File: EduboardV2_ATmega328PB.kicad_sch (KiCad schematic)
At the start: 9 parts, among them J1 EduboardV2 PCIE UP Board Conn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, SW1 K2-1102SP-C4SC-04, U2 ATMEGA328PB-AUR

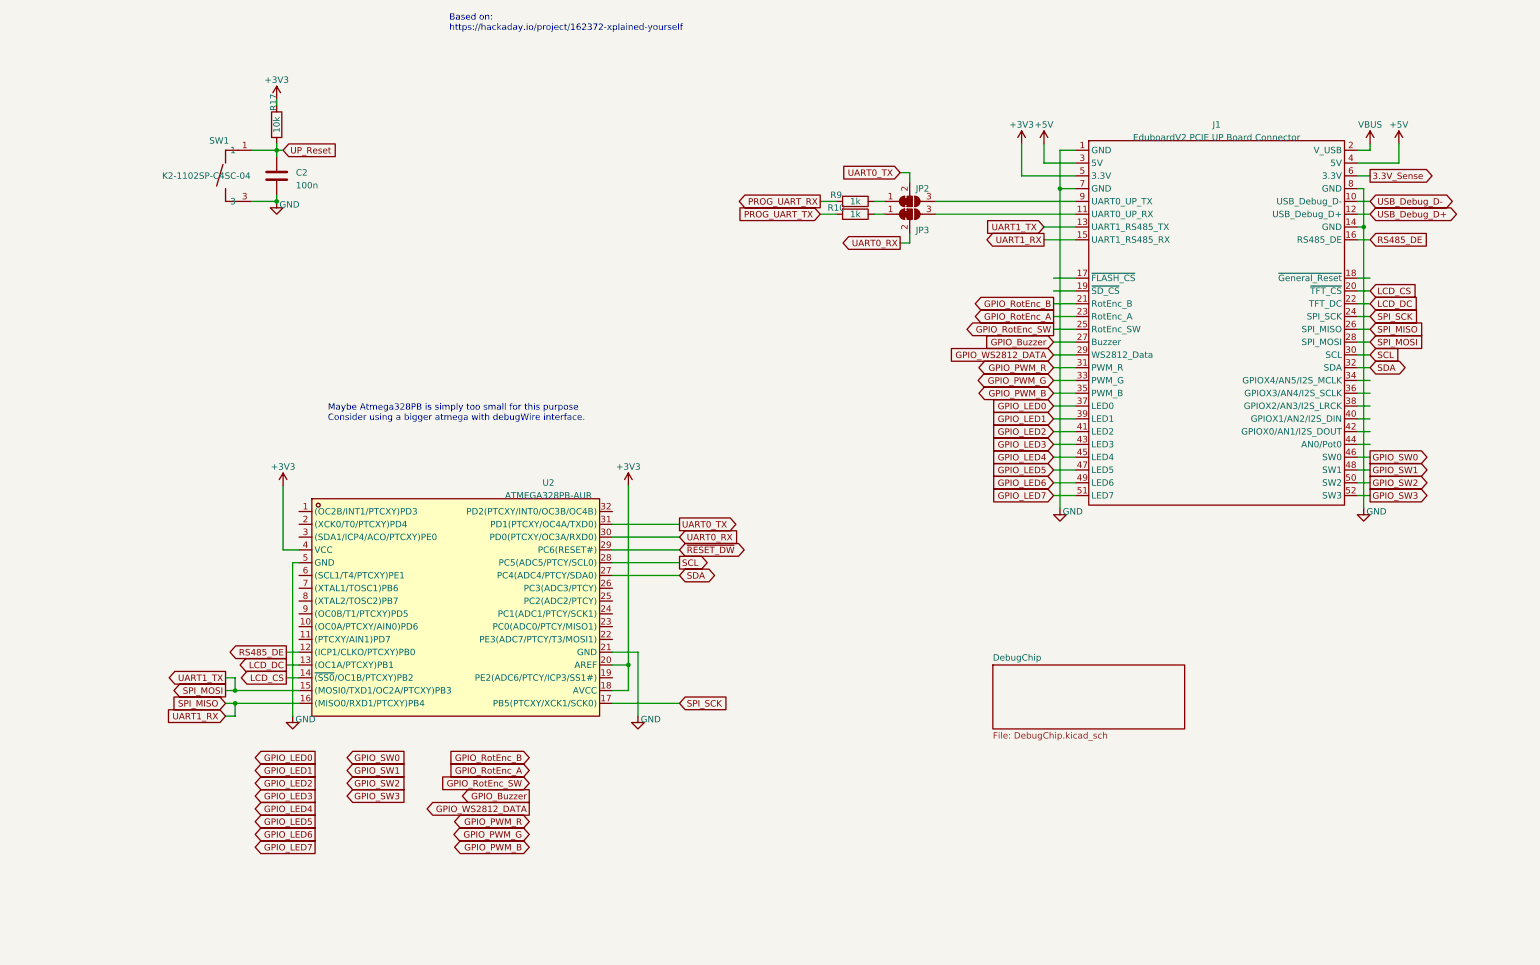
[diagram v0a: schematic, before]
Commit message: start distribute pins to signals.
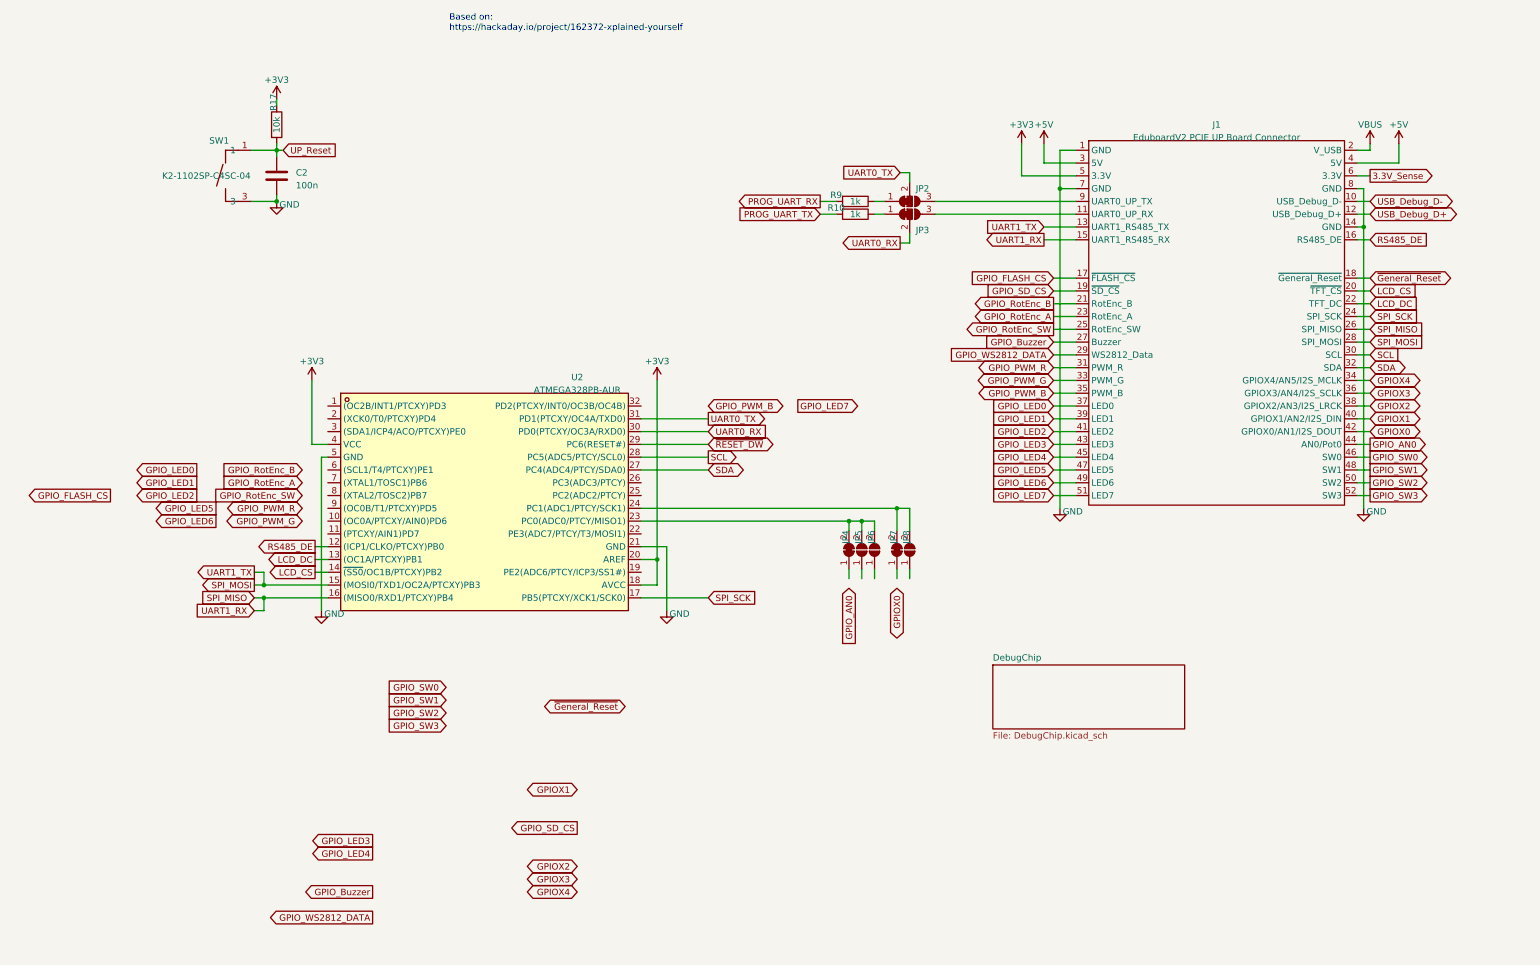
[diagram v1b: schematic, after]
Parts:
- added JP4, JP7: SolderJumper_2_Bridged, symbol Jumper:SolderJumper_2_Bridged
- added JP5, JP6, JP8: SolderJumper_2_Open, symbol Jumper:SolderJumper_2_Open
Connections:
- net GPIO_FLASH_CS: now reaches J1.17 (~{FLASH_CS})
- net ~{General_Reset}: now reaches J1.18 (~{General_Reset})
- net GPIO_SD_CS: now reaches J1.19 (~{SD_CS})
- net GPIOX4: now reaches J1.34 (GPIOX4/AN5/I2S_MCLK)
- net GPIOX3: now reaches J1.36 (GPIOX3/AN4/I2S_SCLK)
- net GPIOX2: now reaches J1.38 (GPIOX2/AN3/I2S_LRCK)
- net GPIOX1: now reaches J1.40 (GPIOX1/AN2/I2S_DIN)
- net GPIOX0: now reaches J1.42 (GPIOX0/AN1/I2S_DOUT)
- net GPIO_AN0: now reaches J1.44 (AN0/Pot0)
- net at U2.23 (PC0(ADC0/PTCY/MISO1)): now also JP4.2 (B), JP5.2 (B), JP6.2 (B)
- net at U2.24 (PC1(ADC1/PTCY/SCK1)): now also JP7.2 (B), JP8.2 (B)
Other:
- note removed: "Maybe Atmega328PB is simply too small for this purpose Consider using a bigger atmega with debugWire interface."
- moved on the sheet: U2

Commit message: schematic done. layout done aswell. Have to check everything trice
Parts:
- removed C2: 100n, Capacitor_SMD:C_0603_1608Metric, symbol Device:C
- removed JP4, JP7: SolderJumper_2_Bridged, symbol Jumper:SolderJumper_2_Bridged
- removed JP5, JP6, JP8: SolderJumper_2_Open, symbol Jumper:SolderJumper_2_Open
- added C1 (x3): 100n, Capacitor_SMD:C_0402_1005Metric, symbol Device:C
- added JP16, JP17, JP18, JP19, JP20, JP21, JP22, JP30, JP34, JP5, JP6, JP7: SolderJumper_3_Bridged12, EduboardV2_kicadlib:SolderJumper_Small-3_bridged12, symbol EduboardV2_kicadlib:SolderJumper_Small_3_Bridged12
- added JP23, JP4: SolderJumper_3_Bridged12, EduboardV2_kicadlib:SolderJumper_Small-4_bridged14, symbol EduboardV2_kicadlib:SolderJumper_Small_4_Bridged14
- JP2, JP3: footprint (none) -> EduboardV2_kicadlib:SolderJumper_Small-3_bridged12
- R10, R17, R9: footprint Resistor_SMD:R_0603_1608Metric -> Resistor_SMD:R_0402_1005Metric
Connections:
- net UP_Reset is gone; now on net ~{RESET_DW}: R17.2, SW1.1, SW1.2
- net +3V3: now also C1.1, C1.1, C1.1
- net GND: now also C1.2, C1.2, C1.2
- net GPIOX0: now also JP4.2 (A)
- net GPIOX1: now also JP5.3 (B)
- net GPIOX2: now also JP6.3 (B)
- net GPIOX3: now also JP23.3 (B)
- net GPIOX4: now also JP16.3 (B)
- net GPIO_AN0: now also JP23.1 (A)
- net GPIO_Buzzer: now also JP20.1 (A)
- net GPIO_FLASH_CS: now also JP4.3 (B)
- net GPIO_LED0: now also U2.1 ((OC2B/INT1/PTCXY)PD3)
- net GPIO_LED1: now also U2.2 ((XCK0/T0/PTCXY)PD4)
- net GPIO_LED2: now also U2.3 ((SDA1/ICP4/ACO/PTCXY)PE0)
- net GPIO_LED3: now also JP21.1 (A)
- net GPIO_LED4: now also JP17.1 (A)
- net GPIO_LED5: now also JP19.1 (A)
- net GPIO_LED6: now also JP18.1 (A)
- net GPIO_LED7: now also JP7.1 (A)
- net GPIO_PWM_B: now also JP7.3 (B)
- net GPIO_PWM_G: now also JP18.3 (B)
- net GPIO_PWM_R: now also JP19.3 (B)
- net GPIO_RotEnc_A: now also JP17.3 (B)
- net GPIO_RotEnc_B: now also JP21.3 (B)
- net GPIO_RotEnc_SW: now also JP20.3 (B)
- net GPIO_SD_CS: now also JP23.2 (A)
- net GPIO_SW0: now also U2.19 (PE2(ADC6/PTCY/ICP3/SS1#))
- net GPIO_SW1: now also U2.22 (PE3(ADC7/PTCY/T3/MOSI1))
- net GPIO_SW2: now also JP5.1 (A)
- net GPIO_SW3: now also JP6.1 (A)
- net GPIO_WS2812_DATA: now also U2.11 ((PTCXY/AIN1)PD7)
- net LCD_DC: now also JP16.1 (A); no longer U2.13 ((OC1A/PTCXY)PB1)
- net RS485_DE: now also JP22.3 (B); no longer U2.12 ((ICP1/CLKO/PTCXY)PB0)
- net SPI_MISO: now also JP34.3 (B); no longer J1.15 (UART1_RS485_RX), U2.16 ((MISO0/RXD1/PTCXY)PB4)
- net SPI_MOSI: now also JP30.1 (A); no longer J1.13 (UART1_RS485_TX), U2.15 ((MOSI0/TXD1/OC2A/PTCXY)PB3)
- net ~{General_Reset}: now also JP4.1 (A)
- net at U2.24 (PC1(ADC1/PTCY/SCK1)): now also JP4.4 (C)
- net at U2.23 (PC0(ADC0/PTCY/MISO1)): now also JP23.4 (C)
- net at U2.10 ((OC0A/PTCXY/AIN0)PD6): now also JP18.2 (C)
- net at U2.25 (PC2(ADC2/PTCY)): now also JP5.2 (C)
- net at U2.26 (PC3(ADC3/PTCY)): now also JP6.2 (C)
- net at U2.32 (PD2(PTCXY/INT0/OC3B/OC4B)): now also JP7.2 (C)
- net at U2.6 ((SCL1/T4/PTCXY)PE1): now also JP21.2 (C)
- net at U2.7 ((XTAL1/TOSC1)PB6): now also JP22.2 (C)
- net at U2.8 ((XTAL2/TOSC2)PB7): now also JP20.2 (C)
- net at U2.9 ((OC0B/T1/PTCXY)PD5): now also JP19.2 (C)
- new net: JP30.2 (C), U2.15 ((MOSI0/TXD1/OC2A/PTCXY)PB3)
- new net: JP17.2 (C), U2.12 ((ICP1/CLKO/PTCXY)PB0)
- new net: JP16.2 (C), U2.13 ((OC1A/PTCXY)PB1)
- new net: JP34.2 (C), U2.16 ((MISO0/RXD1/PTCXY)PB4)
- new net EXT_CLK: JP22.1 (A)
- new net UART1_RX: J1.15 (UART1_RS485_RX), JP34.1 (A)
- new net UART1_TX: J1.13 (UART1_RS485_TX), JP30.3 (B)
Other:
- moved on the sheet: J1, JP2, JP3, R10, R17, R9, SW1, U2

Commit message: got first prototypes. Found some errors. not yet corrected, but marked.
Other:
- note added: "Fehler MISO/UART default falsch"
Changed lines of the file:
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@@
     (effects (font (size 1.27 1.27)) (justify left bottom))
+  )
+  (text "Fehler\nMISO/UART default falsch\n" (at 67.31 168.91 90)
+    (effects (font (size 1.27 1.27) (color 255 0 0 1)) (justify right bottom))
   )
   (global_label "USB_Debug_D+" (shape bidirectional) (at 264.16 33.02 0) (fields_autoplaced)

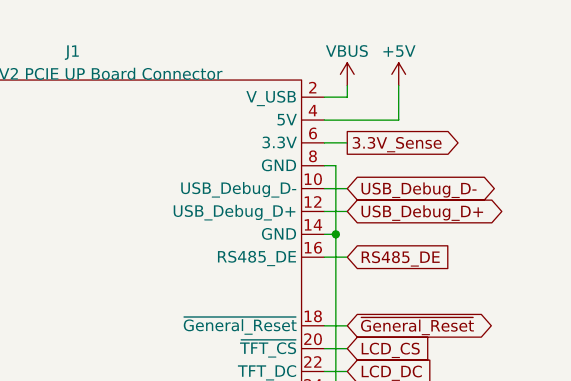
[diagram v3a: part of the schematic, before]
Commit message: remove voltage regulator and change sense input to 3.3V
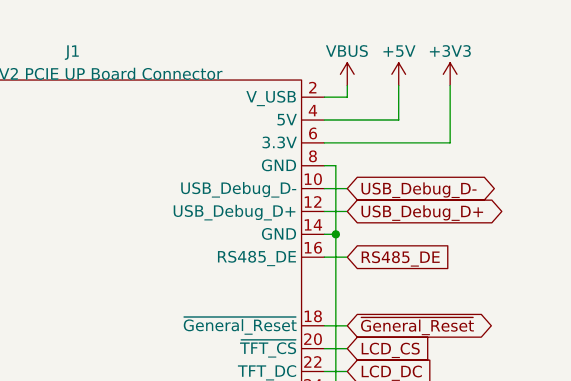
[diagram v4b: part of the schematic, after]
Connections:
- net 3.3V_Sense is gone; now on net +3V3: J1.6 (3.3V)
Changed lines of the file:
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@@
+    (stroke (width 0) (type default))
+  )
+  (wire (pts (xy 275.59 19.05) (xy 275.59 25.4))
     (stroke (width 0) (type default))
   )
@@
     (stroke (width 0) (type default))
   )
-  (wire (pts (xy 261.62 25.4) (xy 264.16 25.4))
+  (wire (pts (xy 261.62 25.4) (xy 275.59 25.4))
     (stroke (width 0) (type default))
   )
@@
     (property "Intersheetrefs" "${INTERSHEET_REFS}" (at 185.4246 68.58 0)
       (effects (font (size 1.27 1.27)) (justify right) hide)
-    )
-  )
-  (global_label "3.3V_Sense" (shape output) (at 264.16 25.4 0) (fields_autoplaced)
-    (effects (font (size 1.27 1.27)) (justify left))
-    (property "Intersheetrefs" "${INTERSHEET_REFS}" (at 277.7096 25.4 0)
-      (effects (font (size 1.27 1.27)) (justify left) hide)
     )
   )
@@
         )
       )
+    )
+  )
+  (symbol (lib_id "power:+3V3") (at 275.59 19.05 0) (unit 1)
+    (in_bom yes) (on_board yes) (dnp no) (fields_autoplaced)
+    (property "Reference" "#PWR04" (at 275.59 22.86 0)
+      (effects (font (size 1.27 1.27)) hide)
+    )
+    (property "Value" "+3V3" (at 275.59 15.24 0)
+      (effects (font (size 1.27 1.27)))
+    )
+    (property "Footprint" "" (at 275.59 19.05 0)
+      (effects (font (size 1.27 1.27)) hide)
+    )
+    (property "Datasheet" "" (at 275.59 19.05 0)
+      (effects (font (size 1.27 1.27)) hide)
+    )
+    (pin "1")
+    (instances
+      (project "EduboardV2_ATmega328PB"
+        (path "/0ef5f433-62f3-413e-ac2a-aa07749066ac/83d3690c-6ff2-4209-82b8-d055572b14ab"
+          (reference "#PWR04") (unit 1)
+        )
+        (path "/0ef5f433-62f3-413e-ac2a-aa07749066ac"
+          (reference "#PWR041") (unit 1)
+        )
+      )

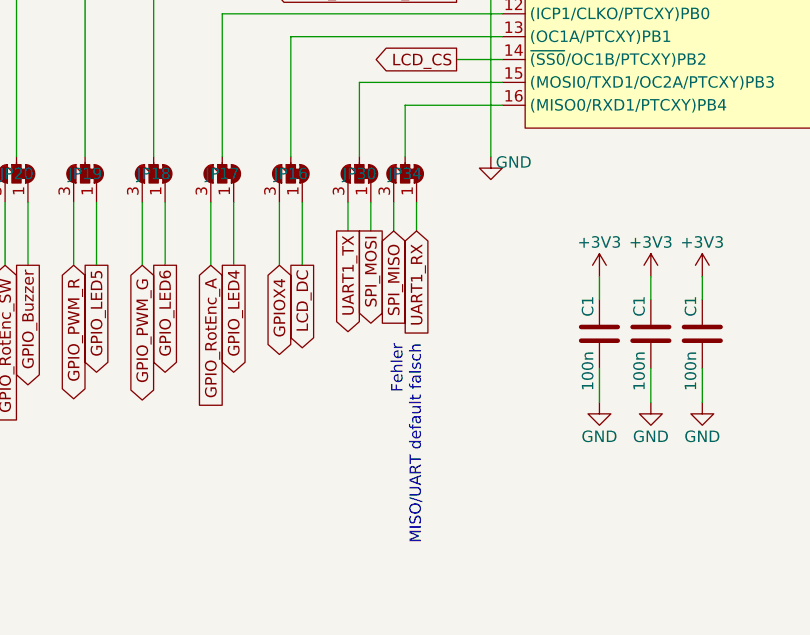
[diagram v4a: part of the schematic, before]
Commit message: switch default routing of j34 miso/uart_rx
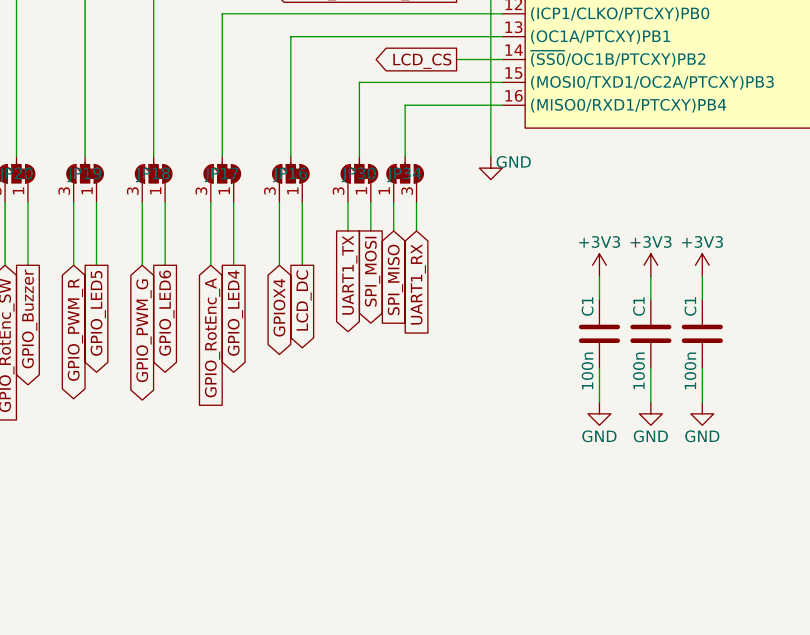
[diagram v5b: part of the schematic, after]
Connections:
- net SPI_MISO: now also JP34.1 (A); no longer JP34.3 (B)
- net UART1_RX: now also JP34.3 (B); no longer JP34.1 (A)
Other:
- note removed: "Fehler MISO/UART default falsch"
- moved on the sheet: JP34
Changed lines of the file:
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@@
     (effects (font (size 1.27 1.27)) (justify left bottom))
-  )
-  (text "Fehler\nMISO/UART default falsch\n" (at 67.31 168.91 90)
-    (effects (font (size 1.27 1.27) (color 255 0 0 1)) (justify right bottom))
   )
   (global_label "USB_Debug_D+" (shape bidirectional) (at 264.16 33.02 0) (fields_autoplaced)
@@
     )
   )
-  (symbol (lib_id "EduboardV2_kicadlib:SolderJumper_Small_3_Bridged12") (at 65.405 149.86 270) (mirror x) (unit 1)
-    (in_bom yes) (on_board yes) (dnp no)
-    (property "Reference" "JP34" (at 67.31 149.86 90)
+  (symbol (lib_id "EduboardV2_kicadlib:SolderJumper_Small_3_Bridged12") (at 65.405 149.86 90) (unit 1)
+    (in_bom yes) (on_board yes) (dnp no)
+    (property "Reference" "JP34" (at 63.5 149.86 90)
       (effects (font (size 1.27 1.27)) (justify right))
     )
-    (property "Value" "SolderJumper_3_Bridged12" (at 72.39 149.86 0)
-      (effects (font (size 1.27 1.27)) hide)
-    )
-    (property "Footprint" "EduboardV2_kicadlib:SolderJumper_Small-3_bridged12" (at 58.42 150.495 0)
-      (effects (font (size 1.27 1.27)) hide)
-    )
+    (property "Value" "SolderJumper_3_Bridged12" (at 58.42 149.86 0)
+      (effects (font (size 1.27 1.27)) hide)
+    )
+    (property "Footprint" "EduboardV2_kicadlib:SolderJumper_Small-3_bridged12" (at 72.39 150.495 0)
+      (effects (font (size 1.27 1.27)) hide)
+    )

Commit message: arrange parts and layout v1.1.
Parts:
- removed JP16, JP17, JP18, JP19, JP20, JP21, JP22, JP30, JP34, JP5, JP6, JP7: SolderJumper_3_Bridged12, EduboardV2_kicadlib:SolderJumper_Small-3_bridged12, symbol EduboardV2_kicadlib:SolderJumper_Small_3_Bridged12
- removed JP2, JP3: SolderJumper_3_Bridged12, EduboardV2_kicadlib:SolderJumper_Small-3_bridged12, symbol Jumper:SolderJumper_3_Bridged12
- removed JP23, JP4: SolderJumper_3_Bridged12, EduboardV2_kicadlib:SolderJumper_Small-4_bridged14, symbol EduboardV2_kicadlib:SolderJumper_Small_4_Bridged14
- added R3 (x32): 0R, Resistor_SMD:R_0603_1608Metric, symbol Device:R
- renumbered U2 to U1
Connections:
- net EXT_CLK: now also R3.1
- net GPIOX0: now also R3.2
- net GPIOX1: now also R3.2
- net GPIOX2: now also R3.2
- net GPIOX3: now also R3.2
- net GPIOX4: now also R3.2
- net GPIO_AN0: now also R3.2
- net GPIO_Buzzer: now also R3.2
- net GPIO_FLASH_CS: now also R3.2
- net GPIO_LED3: now also R3.1
- net GPIO_LED4: now also R3.2
- net GPIO_LED5: now also R3.2
- net GPIO_LED6: now also R3.2
- net GPIO_LED7: now also R3.1
- net GPIO_PWM_B: now also R3.1
- net GPIO_PWM_G: now also R3.2
- net GPIO_PWM_R: now also R3.2
- net GPIO_RotEnc_A: now also R3.2
- net GPIO_RotEnc_B: now also R3.1
- net GPIO_RotEnc_SW: now also R3.2
- net GPIO_SD_CS: now also R3.2
- net GPIO_SW2: now also R3.2
- net GPIO_SW3: now also R3.2
- net LCD_DC: now also R3.2
- net RS485_DE: now also R3.1
- net SPI_MISO: now also R3.2
- net SPI_MOSI: now also R3.2
- net UART0_RX: now also R10.1, R3.1
- net UART0_TX: now also R9.1, R3.1
- net UART1_RX: now also R3.2
- net UART1_TX: now also R3.2
- net ~{General_Reset}: now also R3.2
- net UP_SPI_MOSI: now reaches U1.15 ((MOSI0/TXD1/OC2A/PTCXY)PB3)
- net UP_SPI_MOSI: now also R3.1, R3.1
- net at U1.24 (PC1(ADC1/PTCY/SCK1)): now also R3.1, R3.1, R3.1
- net at U1.12 ((ICP1/CLKO/PTCXY)PB0): now also R3.1, R3.1
- net at J1.9 (UART0_UP_TX): now also R3.2
- net at J1.11 (UART0_UP_RX): now also R3.2
- net at U1.26 (PC3(ADC3/PTCY)): now also R3.1, R3.1
- net at U1.32 (PD2(PTCXY/INT0/OC3B/OC4B)): now also R3.2, R3.2
- net at U1.10 ((OC0A/PTCXY/AIN0)PD6): now also R3.1, R3.1
- net at U1.13 ((OC1A/PTCXY)PB1): now also R3.1, R3.1
- net UP_SPI_MISO: now reaches U1.16 ((MISO0/RXD1/PTCXY)PB4)
- net UP_SPI_MISO: now also R3.1, R3.1
- net at U1.23 (PC0(ADC0/PTCY/MISO1)): now also R3.1, R3.1, R3.1
- net at U1.25 (PC2(ADC2/PTCY)): now also R3.1, R3.1
- net at U1.6 ((SCL1/T4/PTCXY)PE1): now also R3.2, R3.2
- net at U1.7 ((XTAL1/TOSC1)PB6): now also R3.2, R3.2
- net at U1.8 ((XTAL2/TOSC2)PB7): now also R3.1, R3.1
- net at U1.9 ((OC0B/T1/PTCXY)PD5): now also R3.1, R3.1
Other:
- moved on the sheet: R10, R9
